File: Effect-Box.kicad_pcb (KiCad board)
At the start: 6 copper layers, 178.6 x 140 mm, 161 parts, among them J1 Conn_02x07_Odd_Even, J10 Power pins, J2 26642801RP2, J3 FH12A-10S-0.5SH55, J5 Conn_ARM_JTAG_SWD_20, J6 26642801RP2, J7 AudioJack3, J8 AudioJack3, J9 PJ-006A-SMT, SW0 SW_Push, SW1 SW_Push, SW2 SW_Push, SW3 SW_Push, SW4 SW_Push, SW5 SW_Push, SW6 SW_Push, U1 TPS54325, U10 LM7805SX_NOPB, U2 TPS54294, U3 XC7A100T-FTG256, U4 S25FL1, U5 SiT2024B, U7 EFM32GG942F1024, U8 INA1651IPW, U9 PCM3003E

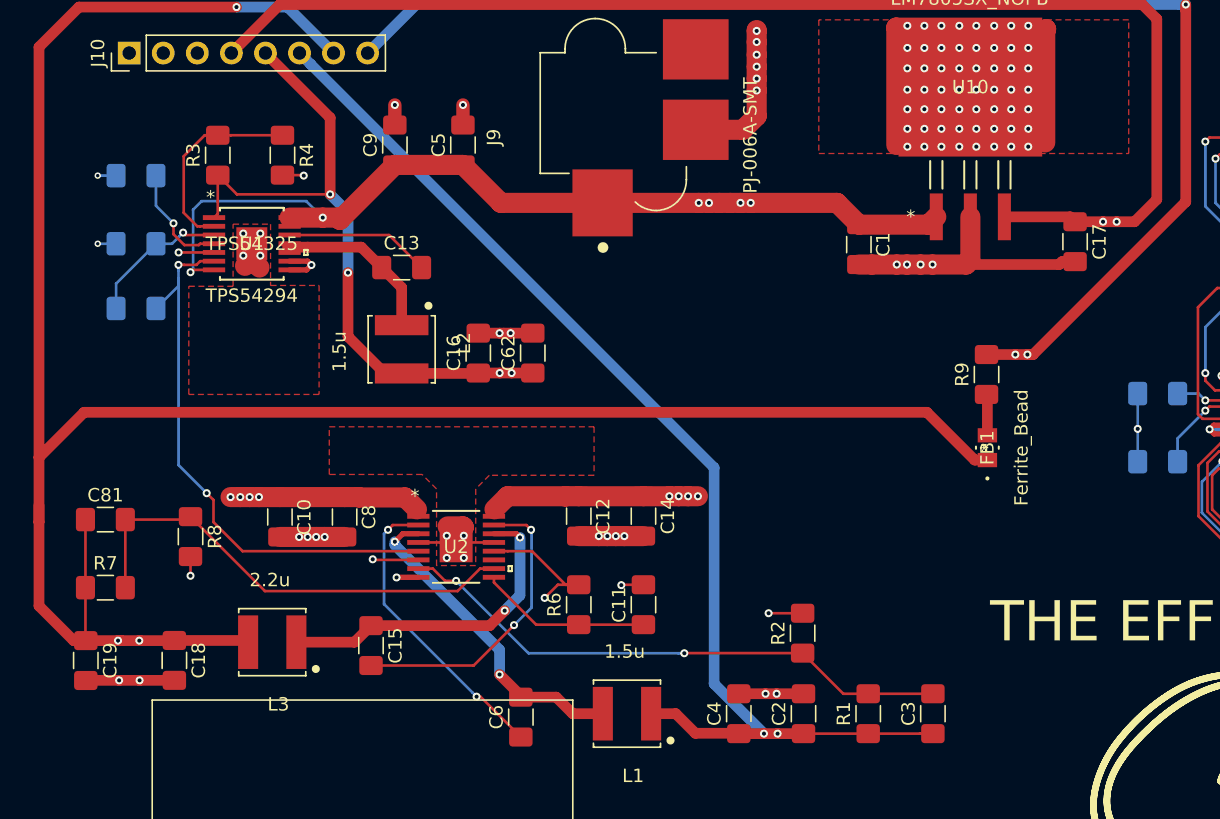
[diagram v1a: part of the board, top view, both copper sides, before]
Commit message: Add more power output vias
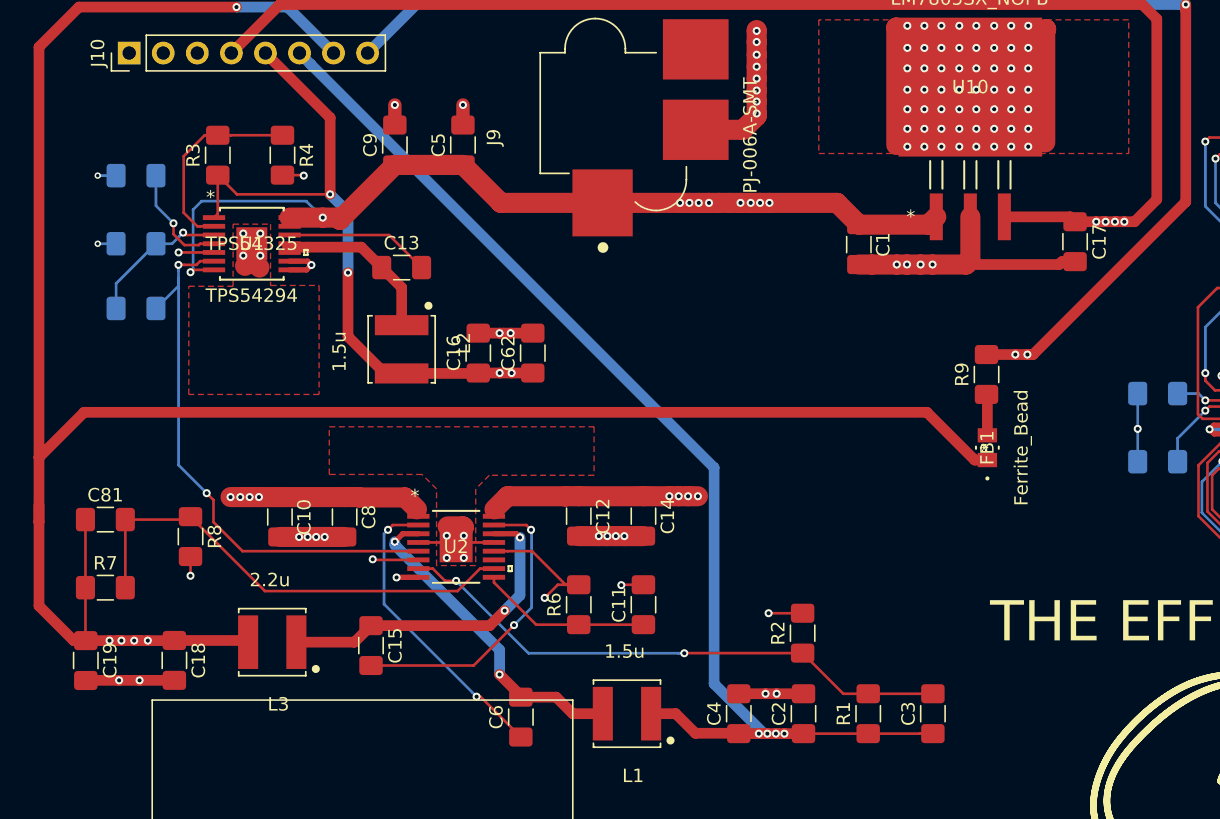
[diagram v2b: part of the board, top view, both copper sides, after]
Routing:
- net GND: vias 220 -> 222
- net +3V3: vias 45 -> 47
- net PWR_IN: vias 14 -> 18
- net +5VA: vias 3 -> 5
- net +1V8: vias 13 -> 15

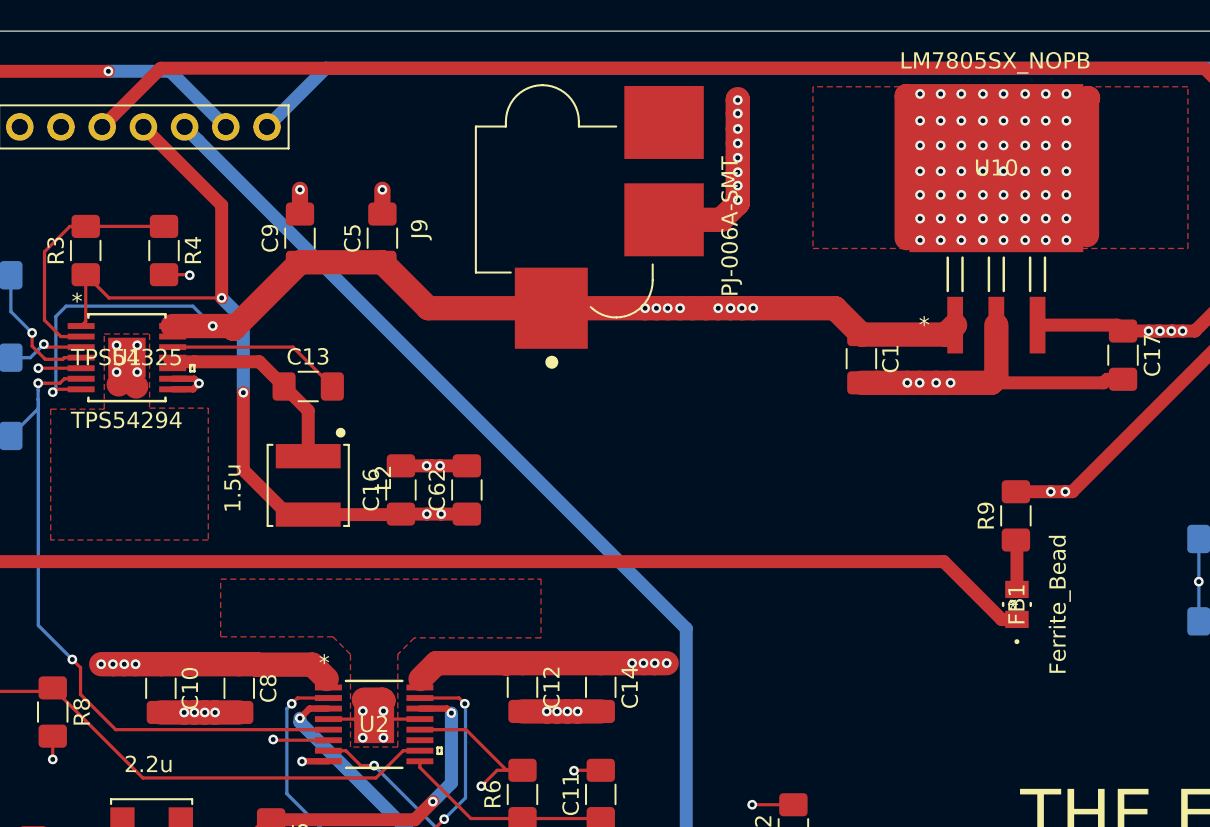
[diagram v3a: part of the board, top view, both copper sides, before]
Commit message: Add more vreg pad thermal vias
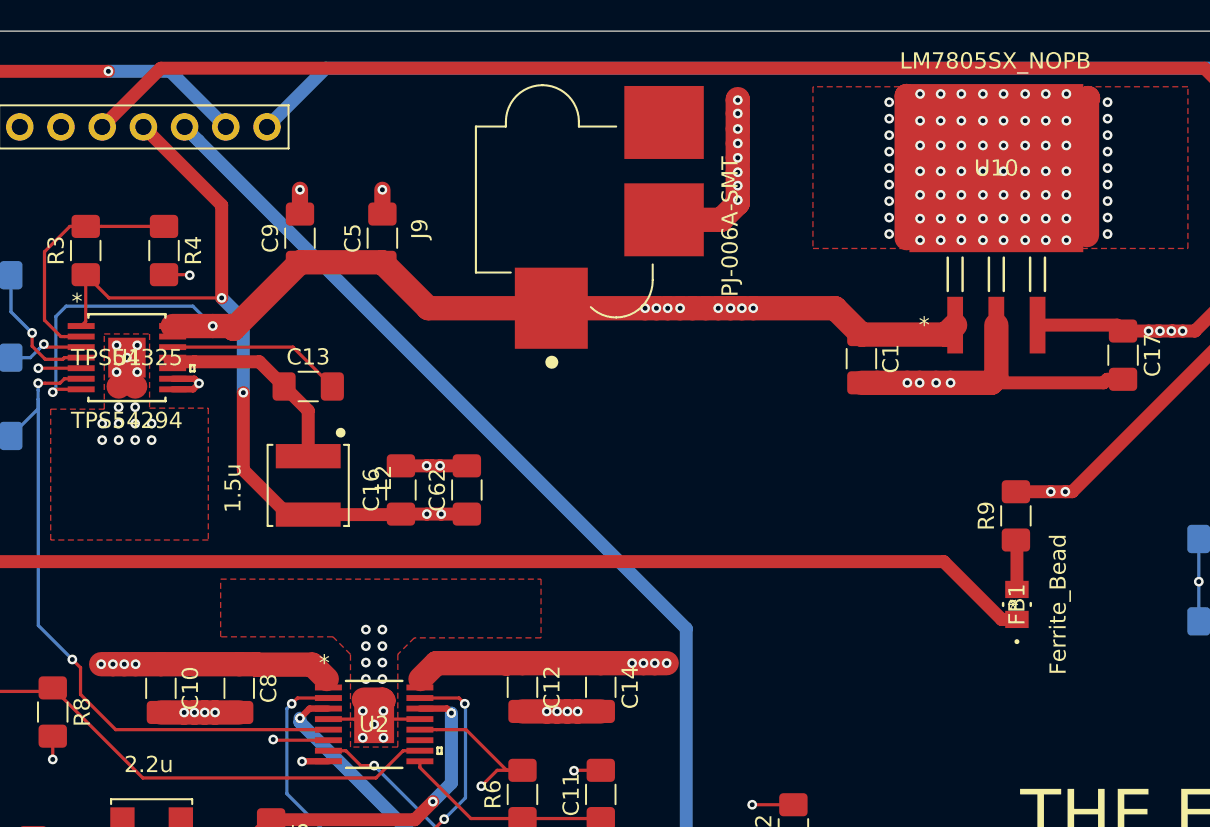
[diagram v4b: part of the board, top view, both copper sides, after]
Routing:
- net GND: track 340.3 -> 340.2 mm, vias 222 -> 260
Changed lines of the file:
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@@
     (thickness 1.6)
     (drawings 3522)
-    (tracks 2399)
+    (tracks 2439)
     (zones 0)
     (modules 161)
@@
   )
   (setup
-    (last_trace_width 0.2)
+    (last_trace_width 1.5)
     (user_trace_width 0.2)
     (user_trace_width 0.4)
@@
   (via (at 151.511 40.782011) (size 0.6) (drill 0.3) (layers F.Cu B.Cu) (net 133))
   (segment (start 154.1526 40.782011) (end 151.511 40.782011) (width 0.2) (layer F.Cu) (net 133))
-  (segment (start 172.212 62.738) (end 172.212 61.849) (width 1.5) (layer F.Cu) (net 133))
+  (segment (start 172.212 62.738) (end 172.212 62.738) (width 1.5) (layer F.Cu) (net 133))
   (segment (start 172.212 61.849) (end 172.7835 61.2775) (width 1.5) (layer F.Cu) (net 133))
   (segment (start 172.7835 61.2775) (end 172.72 61.214) (width 1.5) (layer F.Cu) (net 133))
   (segment (start 172.72 61.214) (end 171.577 61.214) (width 1.5) (layer F.Cu) (net 133))
-  (segment (start 156.972 40.132) (end 156.972 41.275) (width 1.5) (layer F.Cu) (net 133))
-  (segment (start 156.972 41.275) (end 156.464 41.783) (width 1.5) (layer F.Cu) (net 133))
-  (segment (start 156.972 40.132) (end 156.972 41.3385) (width 1.5) (layer F.Cu) (net 133))
-  (segment (start 156.972 41.3385) (end 157.5435 41.91) (width 1.5) (layer F.Cu) (net 133))
+  (segment (start 156.972 40.132) (end 156.972 40.132) (width 1.5) (layer F.Cu) (net 133))
   (segment (start 210.566 28.448) (end 209.4865 28.448) (width 1.5) (layer F.Cu) (net 133))
   (segment (start 209.4865 28.448) (end 205.0415 24.003) (width 1.5) (layer F.Cu) (net 133))
@@
   (segment (start 194.6275 30.4165) (end 194.6275 29.5275) (width 1.5) (layer F.Cu) (net 133))
   (via (at 194.6275 30.4165) (size 0.6) (drill 0.3) (layers F.Cu B.Cu) (net 133))
+  (via (at 171.704 59.944) (size 0.6) (drill 0.3) (layers F.Cu B.Cu) (net 133))
+  (via (at 172.72 59.944) (size 0.6) (drill 0.3) (layers F.Cu B.Cu) (net 133))
+  (via (at 172.72 58.928) (size 0.6) (drill 0.3) (layers F.Cu B.Cu) (net 133))
+  (via (at 171.704 58.928) (size 0.6) (drill 0.3) (layers F.Cu B.Cu) (net 133))
+  (via (at 171.704 57.912) (size 0.6) (drill 0.3) (layers F.Cu B.Cu) (net 133))
+  (via (at 172.72 57.912) (size 0.6) (drill 0.3) (layers F.Cu B.Cu) (net 133))
+  (via (at 156.972 40.132) (size 0.6) (drill 0.3) (layers F.Cu B.Cu) (net 133))
+  (segment (start 172.212 62.738) (end 172.212 61.849) (width 1.5) (layer F.Cu) (net 133))
+  (via (at 172.212 62.738) (size 0.6) (drill 0.3) (layers F.Cu B.Cu) (net 133))
+  (segment (start 156.972 40.132) (end 156.972 41.148) (width 1.5) (layer F.Cu) (net 133))
+  (segment (start 156.972 40.132) (end 156.972 41.402) (width 1.5) (layer F.Cu) (net 133))
+  (segment (start 156.972 41.402) (end 156.464 41.91) (width 1.5) (layer F.Cu) (net 133))
+  (segment (start 156.972 41.402) (end 157.48 41.91) (width 1.5) (layer F.Cu) (net 133))
+  (via (at 157.48 43.18) (size 0.6) (drill 0.3) (layers F.Cu B.Cu) (net 133))
+  (via (at 156.464 43.18) (size 0.6) (drill 0.3) (layers F.Cu B.Cu) (net 133))
+  (via (at 156.464 44.196) (size 0.6) (drill 0.3) (layers F.Cu B.Cu) (net 133))
+  (via (at 157.48 44.196) (size 0.6) (drill 0.3) (layers F.Cu B.Cu) (net 133))
+  (via (at 157.48 45.212) (size 0.6) (drill 0.3) (layers F.Cu B.Cu) (net 133))
+  (via (at 156.464 45.212) (size 0.6) (drill 0.3) (layers F.Cu B.Cu) (net 133))
+  (via (at 155.448 44.196) (size 0.6) (drill 0.3) (layers F.Cu B.Cu) (net 133))
+  (via (at 155.448 45.212) (size 0.6) (drill 0.3) (layers F.Cu B.Cu) (net 133))
+  (via (at 158.496 44.196) (size 0.6) (drill 0.3) (layers F.Cu B.Cu) (net 133))
+  (via (at 158.496 45.212) (size 0.6) (drill 0.3) (layers F.Cu B.Cu) (net 133))
+  (via (at 171.704 56.896) (size 0.6) (drill 0.3) (layers F.Cu B.Cu) (net 133))
+  (via (at 172.72 56.896) (size 0.6) (drill 0.3) (layers F.Cu B.Cu) (net 133))
+  (via (at 217.424 32.512) (size 0.6) (drill 0.3) (layers F.Cu B.Cu) (net 133))
+  (via (at 217.424 31.496) (size 0.6) (drill 0.3) (layers F.Cu B.Cu) (net 133))
+  (via (at 217.424 30.48) (size 0.6) (drill 0.3) (layers F.Cu B.Cu) (net 133))
+  (via (at 217.424 29.464) (size 0.6) (drill 0.3) (layers F.Cu B.Cu) (net 133))
+  (via (at 217.424 28.448) (size 0.6) (drill 0.3) (layers F.Cu B.Cu) (net 133))
+  (via (at 217.424 27.432) (size 0.6) (drill 0.3) (layers F.Cu B.Cu) (net 133))
+  (via (at 217.424 26.416) (size 0.6) (drill 0.3) (layers F.Cu B.Cu) (net 133))
+  (via (at 217.424 25.4) (size 0.6) (drill 0.3) (layers F.Cu B.Cu) (net 133))
+  (via (at 217.424 24.384) (size 0.6) (drill 0.3) (layers F.Cu B.Cu) (net 133))
+  (via (at 203.962 32.512) (size 0.6) (drill 0.3) (layers F.Cu B.Cu) (net 133))
+  (via (at 203.962 31.496) (size 0.6) (drill 0.3) (layers F.Cu B.Cu) (net 133))
+  (via (at 203.962 30.48) (size 0.6) (drill 0.3) (layers F.Cu B.Cu) (net 133))
+  (via (at 203.962 29.464) (size 0.6) (drill 0.3) (layers F.Cu B.Cu) (net 133))
+  (via (at 203.962 28.448) (size 0.6) (drill 0.3) (layers F.Cu B.Cu) (net 133))
+  (via (at 203.962 27.432) (size 0.6) (drill 0.3) (layers F.Cu B.Cu) (net 133))
+  (via (at 203.962 26.416) (size 0.6) (drill 0.3) (layers F.Cu B.Cu) (net 133))
+  (via (at 203.962 25.4) (size 0.6) (drill 0.3) (layers F.Cu B.Cu) (net 133))
+  (via (at 203.962 24.384) (size 0.6) (drill 0.3) (layers F.Cu B.Cu) (net 133))
   (via (at 231.3305 110.6805) (size 0.48) (drill 0.25) (layers F.Cu B.Cu) (net 134))
   (segment (start 230.798 111.18) (end 230.831 111.18) (width 0.2) (layer F.Cu) (net 134))

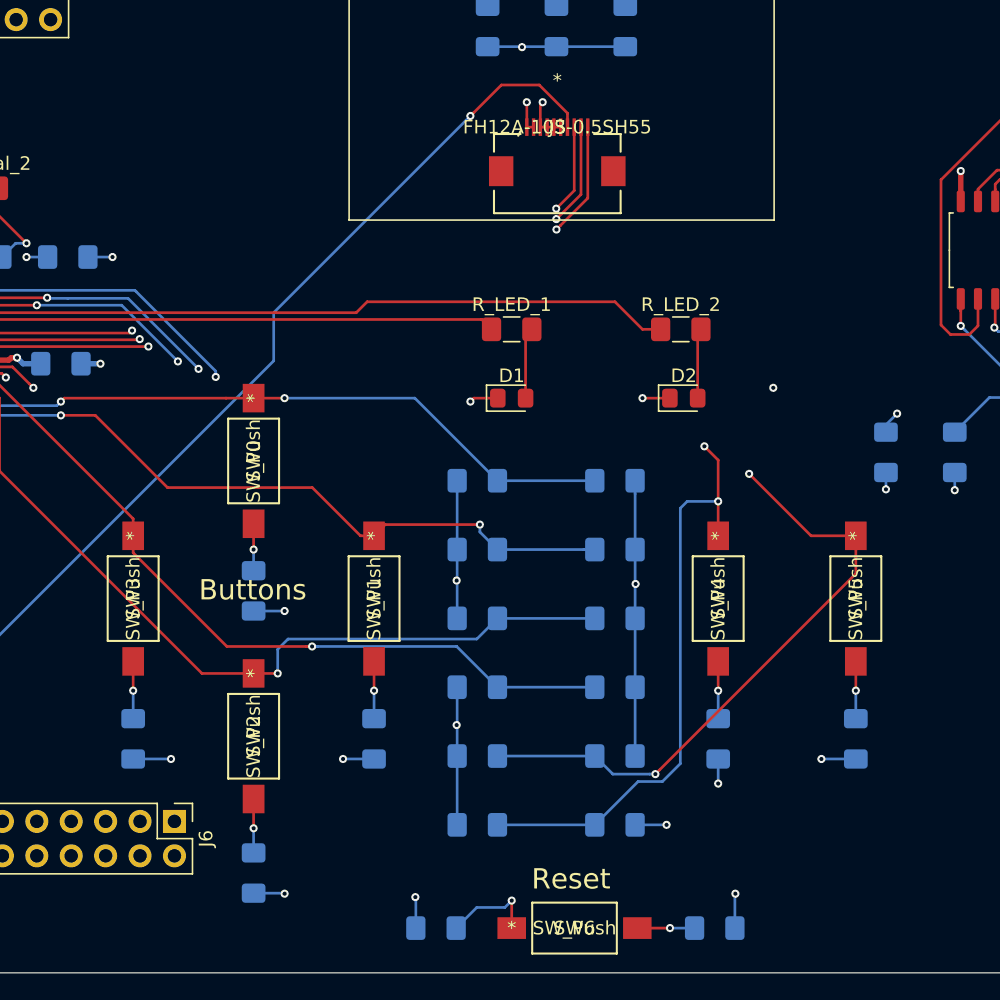
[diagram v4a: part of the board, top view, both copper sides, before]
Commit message: Move silkscreen text away from solder pads
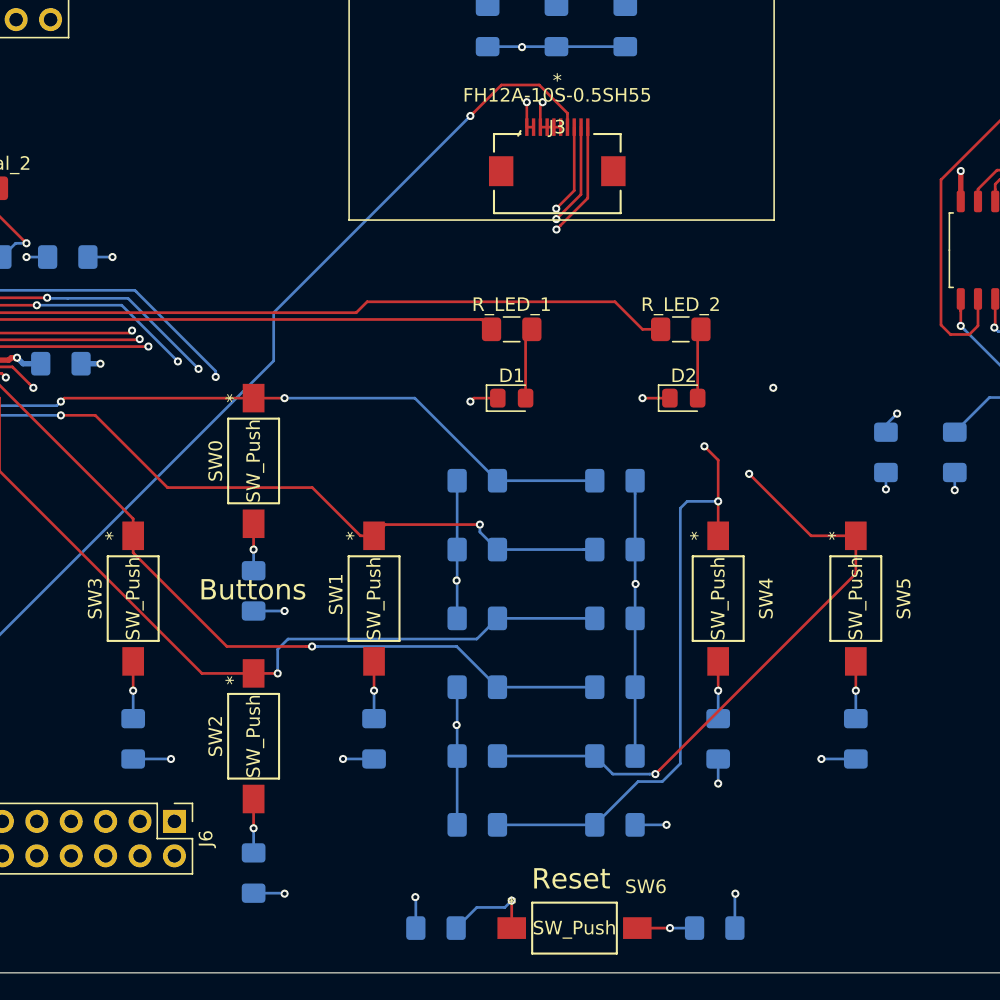
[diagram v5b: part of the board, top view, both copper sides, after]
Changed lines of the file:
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@@
-(kicad_pcb (version 20171130) (host pcbnew "(5.1.4)-1")
+(kicad_pcb (version 20171130) (host pcbnew 5.1.4-e60b266~84~ubuntu16.04.1)
   (general
     (thickness 1.6)
@@
   (page A4)
   (layers
-    (0 F.Cu signal)
+    (0 F.Cu signal hide)
     (1 VCC.Cu power hide)
     (2 In1.Cu signal)
@@
     (37 F.SilkS user)
     (38 B.Mask user)
-    (39 F.Mask user)
+    (39 F.Mask user hide)
     (40 Dwgs.User user hide)
     (41 Cmts.User user hide)
@@
   )
   (setup
-    (last_trace_width 1.5)
+    (last_trace_width 0.2)
     (user_trace_width 0.2)
     (user_trace_width 0.4)
@@
       (effects (font (size 1 1) (thickness 0.15)))
     )
-    (fp_text value FH12A-10S-0.5SH55 (at 0 -3.429) (layer F.SilkS)
+    (fp_text value FH12A-10S-0.5SH55 (at 0 -1.0795) (layer F.SilkS)
       (effects (font (size 1 1) (thickness 0.15)))
     )
@@
   (module button:FSMSMTR (layer F.Cu)
     (at 161.544 156.718 180)
-    (fp_text reference SW6 (at -4.6355 0) (layer F.SilkS)
+    (fp_text reference SW6 (at -9.906 3.048) (layer F.SilkS)
       (effects (font (size 1 1) (thickness 0.15)))
     )
@@
       (effects (font (size 1 1) (thickness 0.15)))
     )
-    (fp_text user * (at 0 0) (layer F.SilkS)
+    (fp_text user * (at 0 1.778) (layer F.SilkS)
       (effects (font (size 1 1) (thickness 0.15)))
     )
@@
   (module button:FSMSMTR (layer F.Cu)
     (at 186.944 127.762 90)
-    (fp_text reference SW5 (at -4.6355 0 90) (layer F.SilkS)
+    (fp_text reference SW5 (at -4.6355 3.556 90) (layer F.SilkS)
       (effects (font (size 1 1) (thickness 0.15)))
     )
@@
       (effects (font (size 1 1) (thickness 0.15)))
     )
-    (fp_text user * (at 0 0 90) (layer F.SilkS)
+    (fp_text user * (at 0 -1.524 90) (layer F.SilkS)
       (effects (font (size 1 1) (thickness 0.15)))
     )
@@
   (module button:FSMSMTR (layer F.Cu)
     (at 176.784 127.762 90)
-    (fp_text reference SW4 (at -4.6355 0 90) (layer F.SilkS)
+    (fp_text reference SW4 (at -4.6355 3.556 90) (layer F.SilkS)
       (effects (font (size 1 1) (thickness 0.15)))
     )
@@
       (effects (font (size 1 1) (thickness 0.15)))
     )
-    (fp_text user * (at 0 0 90) (layer F.SilkS)
+    (fp_text user * (at 0 -1.524 90) (layer F.SilkS)
       (effects (font (size 1 1) (thickness 0.15)))
     )
@@
   (module button:FSMSMTR (layer F.Cu)
     (at 133.604 127.762 90)
-    (fp_text reference SW3 (at -4.6355 0 90) (layer F.SilkS)
+    (fp_text reference SW3 (at -4.6355 -2.794 90) (layer F.SilkS)
       (effects (font (size 1 1) (thickness 0.15)))
     )
@@
       (effects (font (size 0.127 0.127) (thickness 0.002)))
     )
-    (fp_text user * (at 0 0 90) (layer F.SilkS)
+    (fp_text user * (at 0 -1.524 90) (layer F.SilkS)
       (effects (font (size 1 1) (thickness 0.15)))
     )
@@
   (module button:FSMSMTR (layer F.Cu)
     (at 142.494 137.922 90)
-    (fp_text reference SW2 (at -4.6355 0 90) (layer F.SilkS)
+    (fp_text reference SW2 (at -4.6355 -2.794 90) (layer F.SilkS)
       (effects (font (size 1 1) (thickness 0.15)))
     )
@@
       (effects (font (size 1 1) (thickness 0.15)))
     )
-    (fp_text user * (at 0 0 90) (layer F.SilkS)
+    (fp_text user * (at -0.508 -1.524 90) (layer F.SilkS)
       (effects (font (size 1 1) (thickness 0.15)))
     )
@@
   (module button:FSMSMTR (layer F.Cu)
     (at 151.384 127.762 90)
-    (fp_text reference SW1 (at -4.6355 0 90) (layer F.SilkS)
+    (fp_text reference SW1 (at -4.318 -2.794 90) (layer F.SilkS)
       (effects (font (size 1 1) (thickness 0.15)))
     )
@@
       (effects (font (size 1 1) (thickness 0.15)))
     )
-    (fp_text user * (at 0 0 90) (layer F.SilkS)
+    (fp_text user * (at 0 -1.524 90) (layer F.SilkS)
       (effects (font (size 1 1) (thickness 0.15)))
     )
@@
   (module button:FSMSMTR (layer F.Cu)
     (at 142.494 117.602 90)
-    (fp_text reference SW0 (at -4.6355 0 90) (layer F.SilkS)
+    (fp_text reference SW0 (at -4.6355 -2.794 90) (layer F.SilkS)
       (effects (font (size 1 1) (thickness 0.15)))
     )
@@
       (effects (font (size 1 1) (thickness 0.15)))
     )
-    (fp_text user * (at 0 0 90) (layer F.SilkS)
-      (effects (font (size 1 1) (thickness 0.15)))
-    )
+    (fp_text user * (at 0 -1.524 90) (layer F.SilkS)
+      (effects (font (size 1 1) (thickness 0.15)))
+    )
